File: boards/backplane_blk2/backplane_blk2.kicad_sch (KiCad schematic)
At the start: 9 parts, among them J1 Conn_04x24, J2 DIN41612_03x32_C

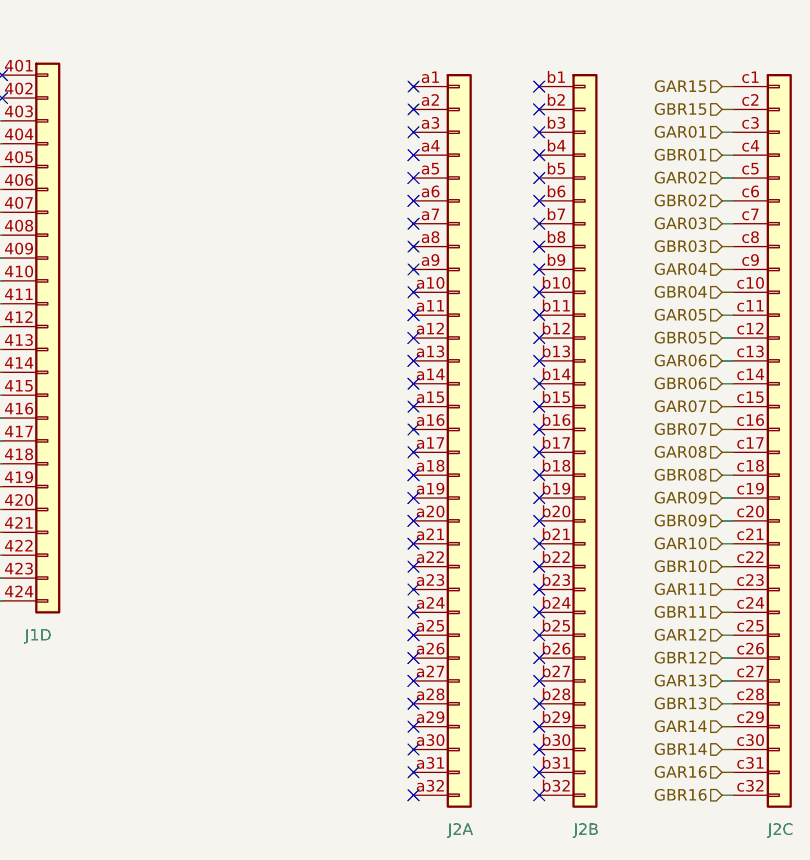
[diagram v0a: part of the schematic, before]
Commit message: Backplane: completed preliminary layout
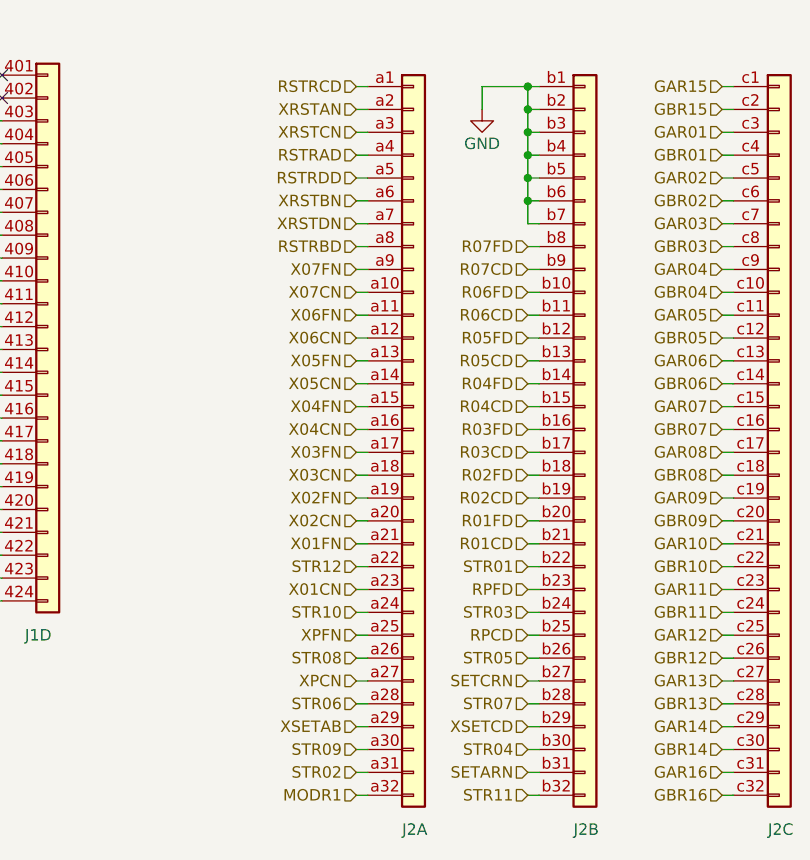
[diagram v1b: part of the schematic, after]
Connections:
- net GND: now also J2.b1, J2.b2, J2.b3, J2.b4, J2.b5, J2.b6, J2.b7
- net MODR1: now also J2.a32
- net R01CD: now also J2.b21
- net R01FD: now also J2.b20
- net R02CD: now also J2.b19
- net R02FD: now also J2.b18
- net R03CD: now also J2.b17
- net R03FD: now also J2.b16
- net R04CD: now also J2.b15
- net R04FD: now also J2.b14
- net R05CD: now also J2.b13
- net R05FD: now also J2.b12
- net R06CD: now also J2.b11
- net R06FD: now also J2.b10
- net R07CD: now also J2.b9
- net R07FD: now also J2.b8
- net RPCD: now also J2.b25
- net RPFD: now also J2.b23
- net RSTRAD: now also J2.a4
- net RSTRBD: now also J2.a8
- net RSTRCD: now also J2.a1
- net RSTRDD: now also J2.a5
- net SETARN: now also J2.b31
- net SETCRN: now also J2.b27
- net STR01: now also J2.b22
- net STR02: now also J2.a31
- net STR03: now also J2.b24
- net STR04: now also J2.b30
- net STR05: now also J2.b26
- net STR06: now also J2.a28
- net STR07: now also J2.b28
- net STR08: now also J2.a26
- net STR09: now also J2.a30
- net STR10: now also J2.a24
- net STR11: now also J2.b32
- net STR12: now also J2.a22
- net X01CN: now also J2.a23
- net X01FN: now also J2.a21
- net X02CN: now also J2.a20
- net X02FN: now also J2.a19
- net X03CN: now also J2.a18
- net X03FN: now also J2.a17
- net X04CN: now also J2.a16
- net X04FN: now also J2.a15
- net X05CN: now also J2.a14
- net X05FN: now also J2.a13
- net X06CN: now also J2.a12
- net X06FN: now also J2.a11
- net X07CN: now also J2.a10
- net X07FN: now also J2.a9
- net XPCN: now also J2.a27
- net XPFN: now also J2.a25
- net XRSTAN: now also J2.a2
- net XRSTBN: now also J2.a6
- net XRSTCN: now also J2.a3
- net XRSTDN: now also J2.a7
- net XSETAB: now also J2.a29
- net XSETCD: now also J2.b29
- no-connect marks 70 -> 6
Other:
- moved on the sheet: J2A

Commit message: Backplane: a little bit of schematic and silkscreen cleanup
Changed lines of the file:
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@@
   (junction (at 233.68 40.64) (diameter 0) (color 0 0 0 0)
+  )
+  (junction (at 172.72 25.4) (diameter 0) (color 0 0 0 0)
   )
   (no_connect (at 58.42 24.13))
@@
     (stroke (width 0) (type default) (color 0 0 0 0))
   )
+  (wire (pts (xy 92.71 24.13) (xy 99.06 24.13))
+    (stroke (width 0) (type default) (color 0 0 0 0))
+  )
   (wire (pts (xy 58.42 31.75) (xy 57.15 31.75))
     (stroke (width 0) (type default) (color 0 0 0 0))
@@
     (stroke (width 0) (type default) (color 0 0 0 0))
   )
+  (wire (pts (xy 88.9 19.05) (xy 92.71 19.05))
+    (stroke (width 0) (type default) (color 0 0 0 0))
+  )
   (wire (pts (xy 78.74 49.53) (xy 77.47 49.53))
     (stroke (width 0) (type default) (color 0 0 0 0))
@@
     (stroke (width 0) (type default) (color 0 0 0 0))
   )
-  (wire (pts (xy 99.06 24.13) (xy 92.71 24.13))
-    (stroke (width 0) (type default) (color 0 0 0 0))
-  )
   (wire (pts (xy 200.66 48.26) (xy 199.39 48.26))
     (stroke (width 0) (type default) (color 0 0 0 0))
@@
     (stroke (width 0) (type default) (color 0 0 0 0))
   )
-  (wire (pts (xy 92.71 17.78) (xy 88.9 17.78))
-    (stroke (width 0) (type default) (color 0 0 0 0))
-  )
   (wire (pts (xy 177.8 25.4) (xy 179.07 25.4))
     (stroke (width 0) (type default) (color 0 0 0 0))
@@
     (stroke (width 0) (type default) (color 0 0 0 0))
   )
+  (wire (pts (xy 88.9 19.05) (xy 88.9 20.32))
+    (stroke (width 0) (type default) (color 0 0 0 0))
+  )
   (wire (pts (xy 158.75 27.94) (xy 160.02 27.94))
     (stroke (width 0) (type default) (color 0 0 0 0))
@@
     (stroke (width 0) (type default) (color 0 0 0 0))
   )
-  (wire (pts (xy 88.9 17.78) (xy 88.9 19.05))
-    (stroke (width 0) (type default) (color 0 0 0 0))
-  )
   (wire (pts (xy 160.02 99.06) (xy 158.75 99.06))
     (stroke (width 0) (type default) (color 0 0 0 0))
@@
     (stroke (width 0) (type default) (color 0 0 0 0))
   )
+  (wire (pts (xy 92.71 19.05) (xy 92.71 24.13))
+    (stroke (width 0) (type default) (color 0 0 0 0))
+  )
   (wire (pts (xy 58.42 44.45) (xy 57.15 44.45))
     (stroke (width 0) (type default) (color 0 0 0 0))
@@
     (stroke (width 0) (type default) (color 0 0 0 0))
   )
+  (wire (pts (xy 172.72 24.13) (xy 172.72 25.4))
+    (stroke (width 0) (type default) (color 0 0 0 0))
+  )
   (wire (pts (xy 119.38 39.37) (xy 118.11 39.37))
     (stroke (width 0) (type default) (color 0 0 0 0))
@@
     (stroke (width 0) (type default) (color 0 0 0 0))
   )
-  (wire (pts (xy 92.71 24.13) (xy 92.71 17.78))
-    (stroke (width 0) (type default) (color 0 0 0 0))
-  )
   (wire (pts (xy 78.74 46.99) (xy 77.47 46.99))
     (stroke (width 0) (type default) (color 0 0 0 0))
@@
   (wire (pts (xy 200.66 68.58) (xy 199.39 68.58))
     (stroke (width 0) (type default) (color 0 0 0 0))
-  )
-  (label "CASE" (at 92.71 24.13 0)
-    (effects (font (size 1.27 1.27)) (justify left bottom))
   )
   (hierarchical_label "GAR08" (shape input) (at 199.39 66.04 180)
@@
     (pin "424")
   )
-  (symbol (lib_id "lachesis:Conn_04x24") (at 83.82 52.07 0) (unit 2)
+  (symbol (lib_name "Conn_04x24_3") (lib_id "lachesis:Conn_04x24") (at 83.82 52.07 0) (unit 2)
     (in_bom yes) (on_board yes)
     (property "Reference" "J1" (id 0) (at 81.28 86.36 0)
@@
     (pin "424")
   )
-  (symbol (lib_id "lachesis:Conn_04x24") (at 104.14 52.07 0) (unit 3)
+  (symbol (lib_name "Conn_04x24_2") (lib_id "lachesis:Conn_04x24") (at 104.14 52.07 0) (unit 3)
     (in_bom yes) (on_board yes)
     (property "Reference" "J1" (id 0) (at 101.6 86.36 0)
@@
     (pin "424")
   )
-  (symbol (lib_id "power:GND") (at 88.9 19.05 0) (unit 1)
-    (in_bom yes) (on_board yes)
-    (property "Reference" "#PWR01" (id 0) (at 88.9 25.4 0)
-      (effects (font (size 1.27 1.27)) hide)
-    )
-    (property "Value" "GND" (id 1) (at 89.027 23.4442 0))
-    (property "Footprint" "" (id 2) (at 88.9 19.05 0)
-      (effects (font (size 1.27 1.27)) hide)
-    )
-    (property "Datasheet" "" (id 3) (at 88.9 19.05 0)
-      (effects (font (size 1.27 1.27)) hide)
-    )
-    (pin "1")
-  )
-  (symbol (lib_id "lachesis:Conn_04x24") (at 124.46 52.07 0) (unit 4)
+  (symbol (lib_name "Conn_04x24_1") (lib_id "lachesis:Conn_04x24") (at 124.46 52.07 0) (unit 4)
     (in_bom yes) (on_board yes)
     (property "Reference" "J1" (id 0) (at 121.92 86.36 0)
@@
     (pin "c9")
   )
-  (symbol (lib_id "lachesis:DIN41612_03x32_C") (at 184.15 53.34 0) (unit 2)
+  (symbol (lib_name "DIN41612_03x32_C_1") (lib_id "lachesis:DIN41612_03x32_C") (at 184.15 53.34 0) (unit 2)
     (in_bom yes) (on_board yes)
     (property "Reference" "J2" (id 0) (at 182.88 107.95 0)
@@
     (pin "c9")
   )
-  (symbol (lib_id "lachesis:DIN41612_03x32_C") (at 205.74 53.34 0) (unit 3)
+  (symbol (lib_name "DIN41612_03x32_C_2") (lib_id "lachesis:DIN41612_03x32_C") (at 205.74 53.34 0) (unit 3)
     (in_bom yes) (on_board yes)
     (property "Reference" "J2" (id 0) (at 204.47 107.95 0)
@@
     (pin "c9")
   )
+  (symbol (lib_id "power:GND") (at 88.9 20.32 0) (unit 1)
+    (in_bom yes) (on_board yes)
+    (property "Reference" "#PWR01" (id 0) (at 88.9 26.67 0)
+      (effects (font (size 1.27 1.27)) hide)
+    )
+    (property "Value" "GND" (id 1) (at 88.9 24.13 0))
+    (property "Footprint" "" (id 2) (at 88.9 20.32 0)
+      (effects (font (size 1.27 1.27)) hide)
+    )
+    (property "Datasheet" "" (id 3) (at 88.9 20.32 0)
+      (effects (font (size 1.27 1.27)) hide)
+    )
+    (pin "1")
+  )
   (symbol (lib_id "Mechanical:MountingHole_Pad") (at 254 36.83 0) (unit 1)
     (in_bom yes) (on_board yes)
@@
     (pin "1")
   )
+  (symbol (lib_id "power:PWR_FLAG") (at 172.72 24.13 0) (unit 1)
+    (in_bom yes) (on_board yes) (fields_autoplaced)
+    (property "Reference" "#FLG01" (id 0) (at 172.72 22.225 0)
+      (effects (font (size 1.27 1.27)) hide)
+    )
+    (property "Value" "PWR_FLAG" (id 1) (at 172.72 19.05 0)
+      (effects (font (size 1.27 1.27)) hide)
+    )
+    (property "Footprint" "" (id 2) (at 172.72 24.13 0)
+      (effects (font (size 1.27 1.27)) hide)
+    )
+    (property "Datasheet" "~" (id 3) (at 172.72 24.13 0)
+      (effects (font (size 1.27 1.27)) hide)
+    )
+    (pin "1")
+  )
   (symbol (lib_id "Mechanical:MountingHole_Pad") (at 259.08 36.83 0) (unit 1)
     (in_bom yes) (on_board yes)
@@
   (symbol (lib_id "power:GND") (at 172.72 27.94 0) (unit 1)
     (in_bom yes) (on_board yes)
-    (property "Reference" "#PWR?" (id 0) (at 172.72 34.29 0)
+    (property "Reference" "#PWR02" (id 0) (at 172.72 34.29 0)
       (effects (font (size 1.27 1.27)) hide)
     )
@@
   (symbol (lib_id "power:GND") (at 243.84 41.91 0) (unit 1)
     (in_bom yes) (on_board yes) (fields_autoplaced)
-    (property "Reference" "#PWR02" (id 0) (at 243.84 48.26 0)
+    (property "Reference" "#PWR03" (id 0) (at 243.84 48.26 0)
       (effects (font (size 1.27 1.27)) hide)
     )
@@
   )
   (symbol_instances
-    (path "/00000000-0000-0000-0000-0000617e1c61"
+    (path "/7adc5225-a8e9-4f66-b509-bcbe687b9936"
+      (reference "#FLG01") (unit 1) (value "PWR_FLAG") (footprint "")
+    )
+    (path "/0459fd90-b074-45d7-9f39-9748996f1be9"
       (reference "#PWR01") (unit 1) (value "GND") (footprint "")
     )
+    (path "/ecba72dd-36a2-478c-b2f0-45557f4d8865"
+      (reference "#PWR02") (unit 1) (value "GND") (footprint "")
+    )
     (path "/ecf8e440-47be-49ba-9a6d-9ee05581edfa"
-      (reference "#PWR02") (unit 1) (value "GND") (footprint "")
-    )
-    (path "/ecba72dd-36a2-478c-b2f0-45557f4d8865"
-      (reference "#PWR?") (unit 1) (value "GND") (footprint "")
+      (reference "#PWR03") (unit 1) (value "GND") (footprint "")
     )
     (path "/e8e884d1-ef65-4fd7-a2dd-830d6bc005fb"

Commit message: Backplane: added names for unconnected rope module pins for completeness
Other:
- note added: "BPLSWF"
- note added: "CLROPR"
- note added: "SPARE"
- note added: "TEST"
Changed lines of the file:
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@@
     (stroke (width 0) (type default) (color 0 0 0 0))
+  )
+  (text "CLROPR" (at 57.15 27.305 180)
+    (effects (font (size 1.27 1.27)) (justify right bottom))
+  )
+  (text "SPARE" (at 71.12 83.185 0)
+    (effects (font (size 1.27 1.27)) (justify left bottom))
+  )
+  (text "TEST" (at 52.705 24.765 0)
+    (effects (font (size 1.27 1.27)) (justify left bottom))
+  )
+  (text "TEST" (at 113.665 24.765 0)
+    (effects (font (size 1.27 1.27)) (justify left bottom))
+  )
+  (text "SPARE" (at 91.44 83.185 0)
+    (effects (font (size 1.27 1.27)) (justify left bottom))
+  )
+  (text "BPLSWF" (at 118.11 27.305 180)
+    (effects (font (size 1.27 1.27)) (justify right bottom))
   )
   (hierarchical_label "GAR08" (shape input) (at 199.39 66.04 180)
